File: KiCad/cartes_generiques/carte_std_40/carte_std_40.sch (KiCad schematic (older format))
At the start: 35 parts, among them K1 RS232, P1 ALIM, P2 CAN1, P3 CAN2, U1 7805, U2 CAN_MCP2551, U3 ICD, U4 MAX232, X1 10M

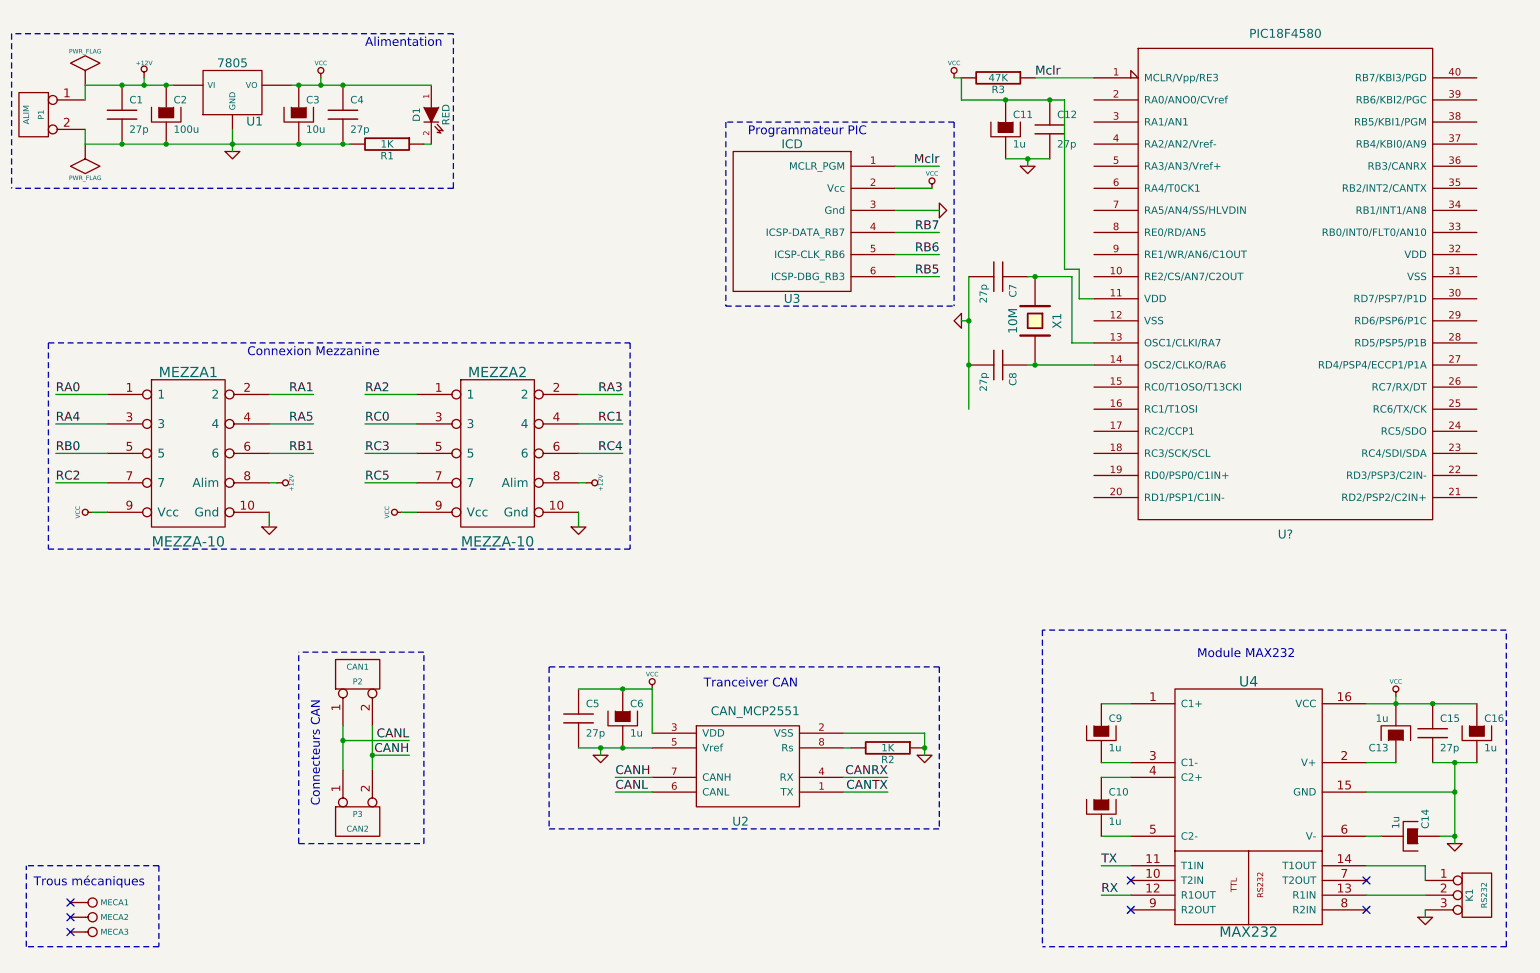
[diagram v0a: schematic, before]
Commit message: création de la carte standard 40
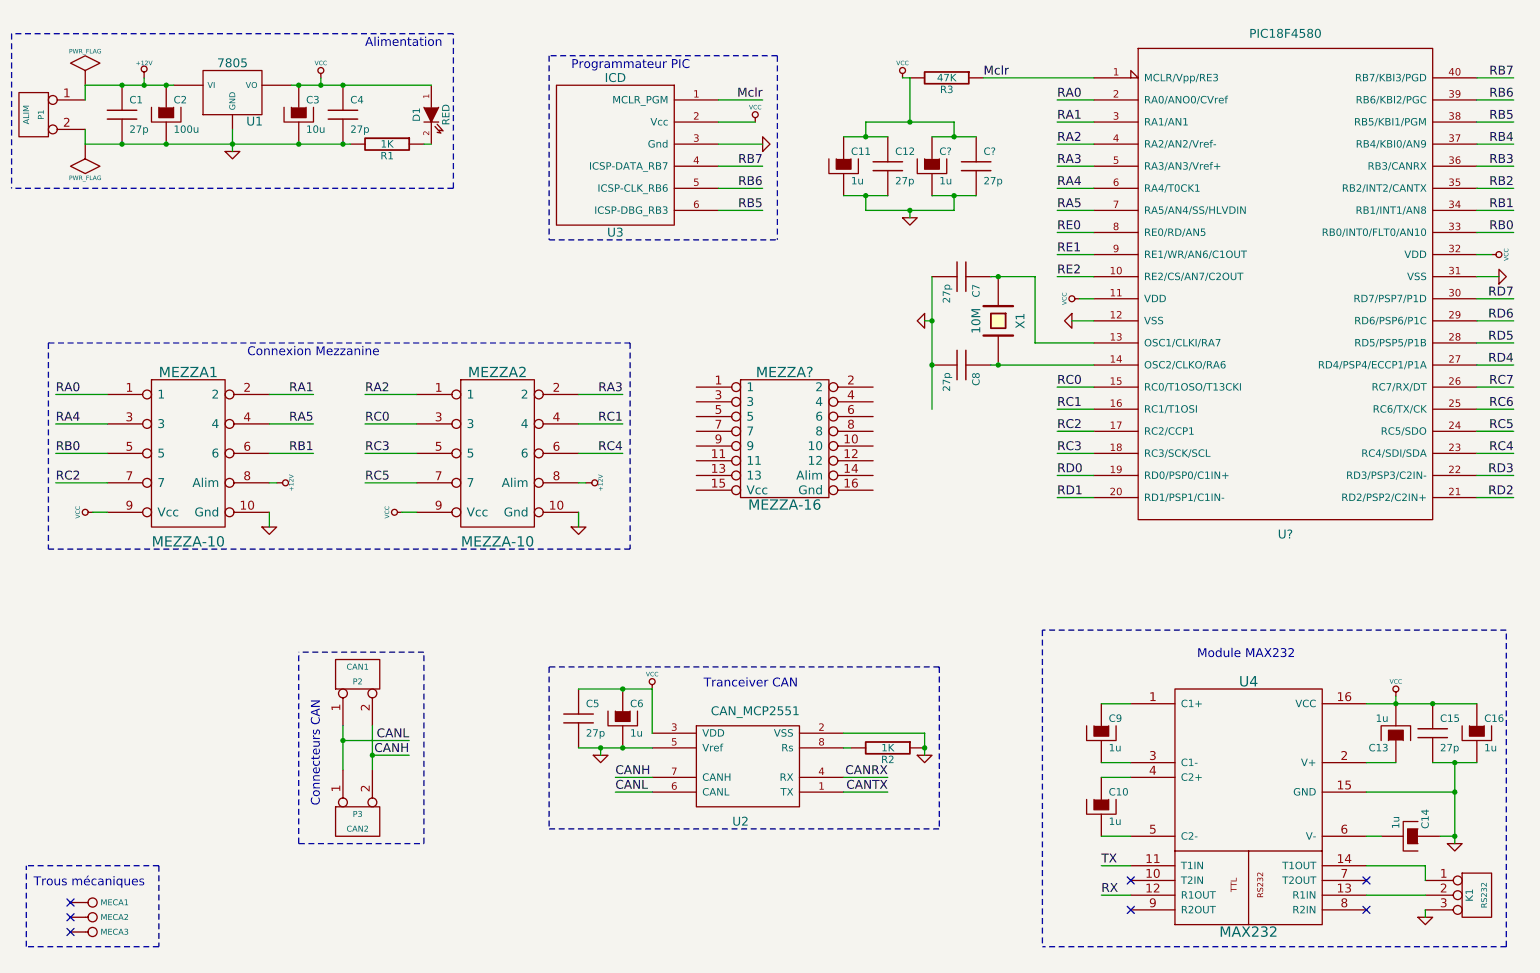
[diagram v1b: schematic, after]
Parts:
- added C?: 1u, symbol CAPAPOL
- added C?: 27p, symbol C
- added MEZZA?: MEZZA-16, symbol MEZZA-16
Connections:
- net GND: now also U?.12 (VSS), U?.31 (VSS), C?.2, C?.2
- net RA0: now also U?.2 (RA0/ANO0/CVref)
- net RA1: now also U?.3 (RA1/AN1)
- net RA2: now also U?.4 (RA2/AN2/Vref-)
- net RA3: now also U?.5 (RA3/AN3/Vref+)
- net RA4: now also U?.6 (RA4/T0CK1)
- net RA5: now also U?.7 (RA5/AN4/SS/HLVDIN)
- net RB0: now also U?.33 (RB0/INT0/FLT0/AN10)
- net RB1: now also U?.34 (RB1/INT1/AN8)
- net RB5: now also U?.38 (RB5/KBI1/PGM)
- net RB6: now also U?.39 (RB6/KBI2/PGC)
- net RB7: now also U?.40 (RB7/KBI3/PGD)
- net RC0: now also U?.15 (RC0/T1OSO/T13CKI)
- net RC1: now also U?.16 (RC1/T1OSI)
- net RC2: now also U?.17 (RC2/CCP1)
- net RC3: now also U?.18 (RC3/SCK/SCL)
- net RC4: now also U?.23 (RC4/SDI/SDA)
- net RC5: now also U?.24 (RC5/SDO)
- net VCC: now also U?.32 (VDD), C?.1, C?.1
- net RE2: now reaches U?.10 (RE2/CS/AN7/C2OUT)
- net RD0: now reaches U?.19 (RD0/PSP0/C1IN+)
- net RD1: now reaches U?.20 (RD1/PSP1/C1IN-)
- net RD2: now reaches U?.21 (RD2/PSP2/C2IN+)
- net RD3: now reaches U?.22 (RD3/PSP3/C2IN-)
- net RC6: now reaches U?.25 (RC6/TX/CK)
- net RC7: now reaches U?.26 (RC7/RX/DT)
- net RD4: now reaches U?.27 (RD4/PSP4/ECCP1/P1A)
- net RD5: now reaches U?.28 (RD5/PSP5/P1B)
- net RD6: now reaches U?.29 (RD6/PSP6/P1C)
- net RD7: now reaches U?.30 (RD7/PSP7/P1D)
- net RB2: now reaches U?.35 (RB2/INT2/CANTX)
- net RB3: now reaches U?.36 (RB3/CANRX)
- net RB4: now reaches U?.37 (RB4/KBI0/AN9)
- net RE0: now reaches U?.8 (RE0/RD/AN5)
- net RE1: now reaches U?.9 (RE1/WR/AN6/C1OUT)
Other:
- moved on the sheet: C11, C12, C7, C8, R3, U3, X1

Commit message: 
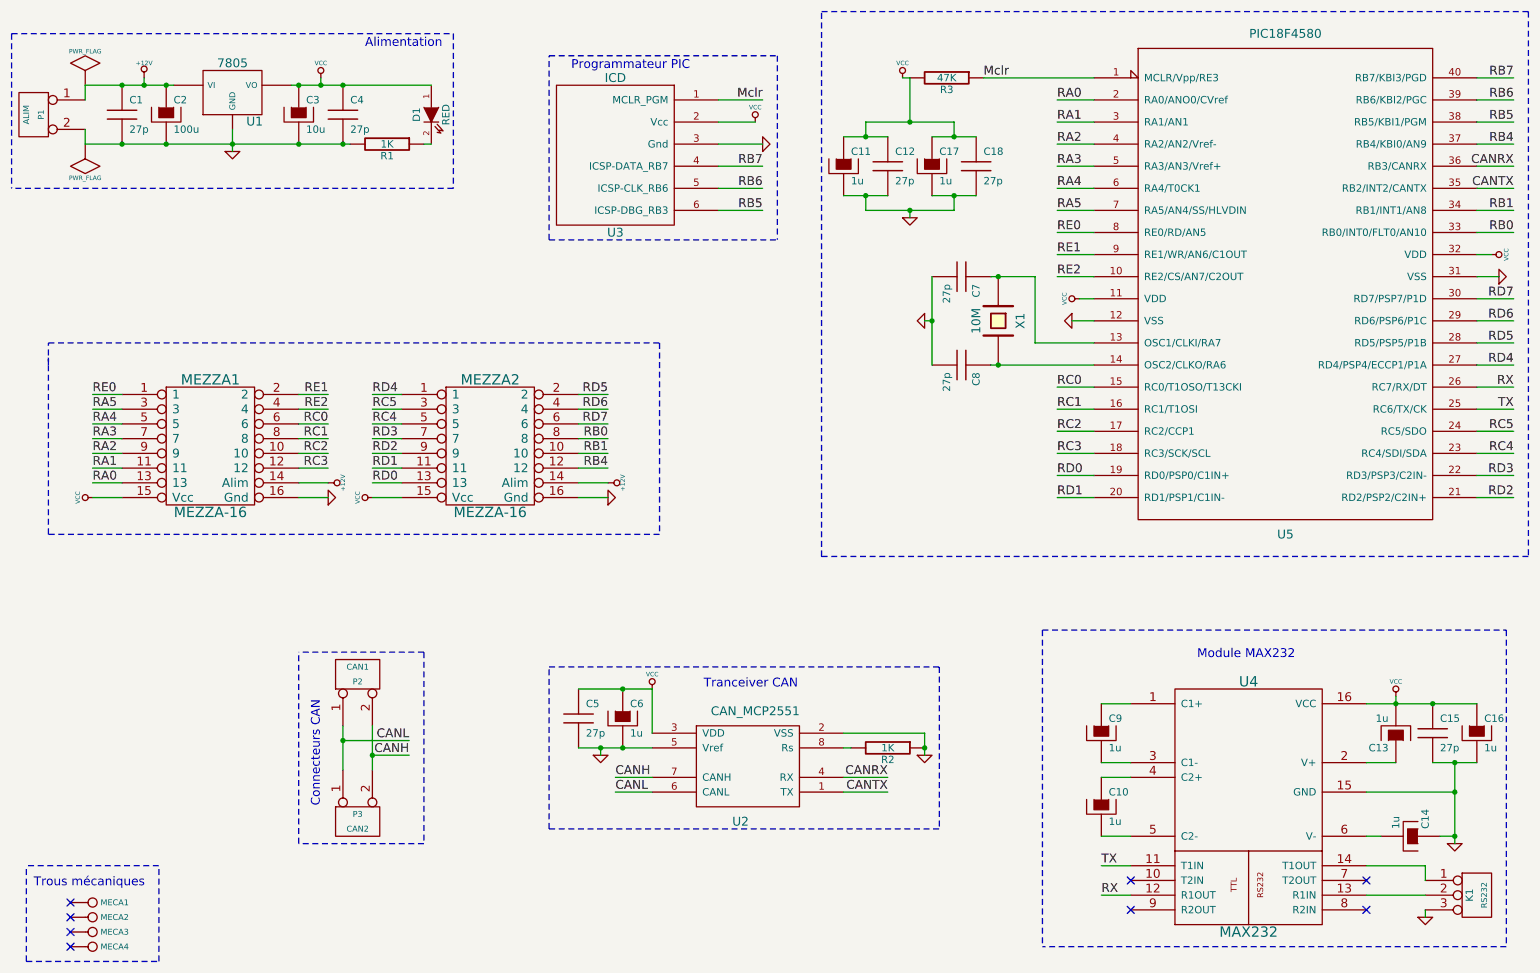
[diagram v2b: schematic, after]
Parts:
- removed MEZZA1, MEZZA2: MEZZA-10, symbol MEZZA-10
- added MECA4: 5mm, symbol CONN_1
- added MEZZA2: MEZZA-16, symbol MEZZA-16
- gave numbers to parts that had none: 4
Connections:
- net RB2 is gone; now on net CANTX: U5.35 (RB2/INT2/CANTX)
- net RB3 is gone; now on net CANRX: U5.36 (RB3/CANRX)
- net RC6 is gone; now on net TX: U5.25 (RC6/TX/CK)
- net RC7 is gone; now on net RX: U5.26 (RC7/RX/DT)
- net +12V: now also MEZZA1.14 (Alim), MEZZA2.14 (Alim)
- net GND: now also MEZZA1.16 (Gnd), MEZZA2.16 (Gnd)
- net RA0: now also MEZZA1.13
- net RA1: now also MEZZA1.11
- net RA2: now also MEZZA1.9
- net RA3: now also MEZZA1.7
- net RA4: now also MEZZA1.5
- net RA5: now also MEZZA1.3
- net RB0: now also MEZZA2.8
- net RB1: now also MEZZA2.10
- net RB4: now also MEZZA2.12
- net RC0: now also MEZZA1.6
- net RC1: now also MEZZA1.8
- net RC2: now also MEZZA1.10
- net RC3: now also MEZZA1.12
- net RC4: now also MEZZA2.5
- net RC5: now also MEZZA2.3
- net RD0: now also MEZZA2.13
- net RD1: now also MEZZA2.11
- net RD2: now also MEZZA2.9
- net RD3: now also MEZZA2.7
- net RD4: now also MEZZA2.1
- net RD5: now also MEZZA2.2
- net RD6: now also MEZZA2.4
- net RD7: now also MEZZA2.6
- net RE0: now also MEZZA1.1
- net RE1: now also MEZZA1.2
- net RE2: now also MEZZA1.4
- net VCC: now also MEZZA1.15 (Vcc), MEZZA2.15 (Vcc)
- no-connect marks 7 -> 8
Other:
- note removed: "Connexion Mezzanine"
- moved on the sheet: MEZZA1
